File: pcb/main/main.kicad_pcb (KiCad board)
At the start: 2 copper layers, 172.1 x 109.2 mm, 74 parts, among them J1 Conn_01x04, J10 JTAG, J2 USB_B, J3 Trackball_conn, J4 ROW0, J5 RJ45, J6 ROW1, J7 ROW2, J8 ROW3, J9 STLink, SW1 SW40, SW2 SW41, SW3 SW42, SW4 SW43, SW5 RST_SW, SW6 BOOT0, SW7 BOOT1, U1 3.3v regul, U2 STM32F103C8Tx, Y1 32.768kHz, Y2 8MHz

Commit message: keyboard pcb
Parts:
- added G***: LOGO, folivora:logo, B.Cu at (189.2, 124.5)
- added G***: LOGO, folivora:logo, F.Cu at (172.7, 78.7)
- added G***: LOGO, folivora:logo, F.Cu at (189.2, 61.0)
- added G***: LOGO, folivora:logo, F.Cu at (189.2, 124.5)
- D5, D6, D7: footprint LED_THT:LED_D3.0mm -> LED_SMD:LED_1206_3216Metric
- moved D5 17.1 mm to (104.8, 105.4), turned to 180 degrees
- moved REF** 12.4 mm to (105.4, 90.2)
- moved D6 10.0 mm to (104.8, 102.9), turned to 180 degrees
- moved J10 5.59 mm to (216.4, 161.0)
- moved D7 3.25 mm to (104.8, 100.3), turned to 180 degrees
- moved R2 2.29 mm to (106.7, 109.2)
- moved J3 1.85 mm to (154.9, 153.0)
- moved R1 1.52 mm to (104.8, 109.2)
- moved C10 0.28 mm to (112.3, 123.4), turned to 90 degrees
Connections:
- J3 pad 1: +3V3 -> GND
- J3 pad 2: /SS_T -> /MOSI
- J3 pad 3: /SCK -> /MISO
- J3 pad 4: /MISO -> /SCK
- J3 pad 5: /MOSI -> /SS_T
- J3 pad 6: GND -> +3V3
- JP12 pad 1: +5V -> +3V3
- JP15 pad 1: +5V -> +3V3
- U2 pad 21: /LED3 -> Net-(U2-Pad21)
- U2 pad 22: /D- -> /READ5
- U2 pad 25: /D+ -> /READ4
- U2 pad 32: /READ5 -> /D-
- U2 pad 33: /READ4 -> /D+
- U2 pad 41: Net-(U2-Pad41) -> /LED3
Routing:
- net GND: track 0.00 -> 364.3 mm, vias 0 -> 11
- net +3V3: track 0.00 -> 345.9 mm, vias 0 -> 12
- net /READ0: track 80.8 -> 272.5 mm, vias 1 -> 7
- net /READ1: track 79.4 -> 269.4 mm, vias 2 -> 16
- net /RST: track 0.00 -> 184.1 mm, vias 0 -> 10
- net /SELECT1: track 0.00 -> 172.8 mm, vias 0 -> 2
- net /READ2: track 83.4 -> 254.0 mm, vias 0 -> 12
- net /READ3: track 86.7 -> 250.9 mm, vias 0 -> 5
- net /SELECT2: track 0.00 -> 161.7 mm, vias 0 -> 9
- net /SELECT4: track 0.00 -> 159.2 mm, vias 0 -> 4
- net /SELECT3: track 0.00 -> 156.6 mm, vias 0 -> 5
- net +5V: track 0.00 -> 154.1 mm, vias 0 -> 8
- net /JTDO: track 0.00 -> 148.1 mm, vias 0 -> 6
- net /BOOT1: track 0.00 -> 146.2 mm, vias 0 -> 2
- net /BOOT0: track 0.00 -> 146.0 mm, vias 0 -> 8
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- added copper zone on B.Cu, net GND
- added copper zone on F.Cu, net GND
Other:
- outline, holes or cut-outs redrawn
- rule trace_min: 0.2 -> 0
- board text added: "0.1uF"
- board text added: "10Mohm"
- board text added: "10kohm"
- board text added: "10uF"
- board text added: "220ohm"
- board text added: "32.768kHz"
- board text added: "8MHz"
- board text added: "<-D"
- board text added: "BOOT0"
- board text added: "BOOT1"
- board text added: "D->"
- board text added: "Fill all if this is ride side"
- board text added: "JTAG 10pin"
- board text added: "RJ45"
- board text added: "RST"
- board text added: "STLink"
- board text added: "STM32F103C8Tx"
- board text added: "Trackball"
- board text added: "USB B"
- board text added: "to 3.3v"

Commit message: fix design
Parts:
- removed the REF** at (263.5, 147.3)
- removed the REF** at (263.5, 128.3)
- removed the REF** at (125.7, 90.2)
- added REF**: MountingHole_2.2mm_M2, MountingHole:MountingHole_2.2mm_M2, F.Cu at (55.9, 72.4)
- added REF**: MountingHole_2.2mm_M2, MountingHole:MountingHole_2.2mm_M2, F.Cu at (74.9, 59.7)
- added REF**: MountingHole_2.2mm_M2, MountingHole:MountingHole_2.2mm_M2, F.Cu at (113.0, 59.7)
- added REF**: MountingHole_2.2mm_M2, MountingHole:MountingHole_2.2mm_M2, F.Cu at (113.0, 72.4)
- added REF**: MountingHole_2.2mm_M2, MountingHole:MountingHole_2.2mm_M2, F.Cu at (55.9, 53.3)
- added REF**: MountingHole_2.2mm_M2, MountingHole:MountingHole_2.2mm_M2, F.Cu at (132.1, 40.6)
- added REF**: MountingHole_2.2mm_M2, MountingHole:MountingHole_2.2mm_M2, F.Cu at (94.0, 53.3)
- added REF**: MountingHole_2.2mm_M2, MountingHole:MountingHole_2.2mm_M2, F.Cu at (94.0, 40.6)
- added REF**: MountingHole_2.2mm_M2, MountingHole:MountingHole_2.2mm_M2, F.Cu at (151.1, 53.3)
- added REF**: MountingHole_2.2mm_M2, MountingHole:MountingHole_2.2mm_M2, F.Cu at (55.9, 40.6)
- added REF**: MountingHole_2.2mm_M2, MountingHole:MountingHole_2.2mm_M2, F.Cu at (151.1, 40.6)
- added REF**: MountingHole_2.2mm_M2, MountingHole:MountingHole_2.2mm_M2, F.Cu at (132.1, 59.7)
- added REF**: MountingHole_2.2mm_M2, MountingHole:MountingHole_2.2mm_M2, F.Cu at (132.1, 53.3)
- added REF**: MountingHole_2.2mm_M2, MountingHole:MountingHole_2.2mm_M2, F.Cu at (74.9, 53.3)
- added REF**: MountingHole_2.2mm_M2, MountingHole:MountingHole_2.2mm_M2, F.Cu at (74.9, 40.6)
- added REF**: MountingHole_2.2mm_M2, MountingHole:MountingHole_2.2mm_M2, F.Cu at (113.0, 40.6)
- added REF**: MountingHole_2.2mm_M2, MountingHole:MountingHole_2.2mm_M2, F.Cu at (113.0, 53.3)
- added REF**: MountingHole_2.2mm_M2, MountingHole:MountingHole_2.2mm_M2, F.Cu at (55.9, 34.3)
- added REF**: MountingHole_2.2mm_M2, MountingHole:MountingHole_2.2mm_M2, F.Cu at (132.1, 21.6)
- added REF**: MountingHole_2.2mm_M2, MountingHole:MountingHole_2.2mm_M2, F.Cu at (94.0, 34.3)
- added REF**: MountingHole_2.2mm_M2, MountingHole:MountingHole_2.2mm_M2, F.Cu at (94.0, 21.6)
- added REF**: MountingHole_2.2mm_M2, MountingHole:MountingHole_2.2mm_M2, F.Cu at (151.1, 34.3)
- added REF**: MountingHole_2.2mm_M2, MountingHole:MountingHole_2.2mm_M2, F.Cu at (94.0, 72.4)
- added REF**: MountingHole_2.2mm_M2, MountingHole:MountingHole_2.2mm_M2, F.Cu at (55.9, 21.6)
- added REF**: MountingHole_2.2mm_M2, MountingHole:MountingHole_2.2mm_M2, F.Cu at (151.1, 21.6)
- added REF**: MountingHole_2.2mm_M2, MountingHole:MountingHole_2.2mm_M2, F.Cu at (132.1, 34.3)
- added REF**: MountingHole_2.2mm_M2, MountingHole:MountingHole_2.2mm_M2, F.Cu at (74.9, 34.3)
- added REF**: MountingHole_2.2mm_M2, MountingHole:MountingHole_2.2mm_M2, F.Cu at (74.9, 21.6)
- added REF**: MountingHole_2.2mm_M2, MountingHole:MountingHole_2.2mm_M2, F.Cu at (113.0, 21.6)
- added REF**: MountingHole_2.2mm_M2, MountingHole:MountingHole_2.2mm_M2, F.Cu at (113.0, 34.3)
- added REF**: MountingHole_2.2mm_M2, MountingHole:MountingHole_2.2mm_M2, F.Cu at (94.0, 59.7)
- added REF**: MountingHole_3.2mm_M3, MountingHole:MountingHole_3.2mm_M3, F.Cu at (161.9, 66.0)
- added REF**: MountingHole_3.2mm_M3, MountingHole:MountingHole_3.2mm_M3, F.Cu at (161.9, 47.0)
- added REF**: MountingHole_3.2mm_M3, MountingHole:MountingHole_3.2mm_M3, F.Cu at (24.1, 5.08)
- added REF**: MountingHole_2.2mm_M2, MountingHole:MountingHole_2.2mm_M2, F.Cu at (55.9, 15.2)
- added REF**: MountingHole_2.2mm_M2, MountingHole:MountingHole_2.2mm_M2, F.Cu at (151.1, 72.4)
- added REF**: MountingHole_2.2mm_M2, MountingHole:MountingHole_2.2mm_M2, F.Cu at (55.9, 2.54)
- added REF**: MountingHole_2.2mm_M2, MountingHole:MountingHole_2.2mm_M2, F.Cu at (74.9, 2.54)
- added REF**: MountingHole_2.2mm_M2, MountingHole:MountingHole_2.2mm_M2, F.Cu at (74.9, 15.2)
- added REF**: MountingHole_2.2mm_M2, MountingHole:MountingHole_2.2mm_M2, F.Cu at (94.0, 2.54)
- added REF**: MountingHole_2.2mm_M2, MountingHole:MountingHole_2.2mm_M2, F.Cu at (94.0, 15.2)
- added REF**: MountingHole_2.2mm_M2, MountingHole:MountingHole_2.2mm_M2, F.Cu at (113.0, 2.54)
- added REF**: MountingHole_2.2mm_M2, MountingHole:MountingHole_2.2mm_M2, F.Cu at (113.0, 15.2)
- added REF**: MountingHole_2.2mm_M2, MountingHole:MountingHole_2.2mm_M2, F.Cu at (55.9, 59.7)
- added REF**: MountingHole_2.2mm_M2, MountingHole:MountingHole_2.2mm_M2, F.Cu at (151.1, 59.7)
- added REF**: MountingHole_2.2mm_M2, MountingHole:MountingHole_2.2mm_M2, F.Cu at (132.1, 72.4)
- added REF**: MountingHole_2.2mm_M2, MountingHole:MountingHole_2.2mm_M2, F.Cu at (74.9, 72.4)
- J4, J6, J7, J8: footprint Connector_JST:JST_XH_S07B-XH-A_1x07_P2.50mm_Horizontal -> Connector_PinSocket_2.00mm:PinSocket_1x07_P2.00mm_Vertical; moved to F.Cu
- SW6, SW7: footprint Button_Switch_THT:SW_E-Switch_EG1224_SPDT_Angled -> Button_Switch_THT:SW_CuK_OS102011MA1QN1_SPDT_Angled
- moved J3 155.8 mm to (21.6, 72.4), turned to 270 degrees
- moved U1 150.0 mm to (19.7, 59.1), turned to 45 degrees
- moved C2 145.1 mm to (15.2, 64.8), turned to 135 degrees
- moved C1 144.7 mm to (10.8, 64.8), turned to 315 degrees
- moved J4 134.3 mm to (132.1, 3.17), turned to 0 degrees
- moved REF** 132.5 mm to (3.81, 5.08)
- moved J2 131.0 mm to (12.7, 16.0)
- moved J6 130.6 mm to (168.3, 21.6), turned to 0 degrees
- moved C5 130.1 mm to (6.35, 47.4)
- moved D5 130.1 mm to (3.17, 24.1)
- moved D6 130.1 mm to (3.17, 21.6)
- moved D7 130.1 mm to (3.17, 19.1)
- moved J1 130.1 mm to (10.2, 21.8)
- moved J9 130.1 mm to (95.5, 79.8)
- moved JP10 130.1 mm to (10.2, 25.7)
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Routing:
- net +3V3: track 345.9 -> 289.7 mm, vias 12 -> 16
- net /MOSI: track 81.3 -> 42.6 mm, vias 2 -> 0
- net /READ5: track 205.5 -> 243.8 mm, vias 2 -> 1
- net /MISO: track 90.1 -> 55.2 mm
- net /READ1: track 269.4 -> 299.2 mm, vias 16 -> 5
- net /READ4: track 208.3 -> 232.3 mm, vias 2 -> 4
- net /READ2: track 254.0 -> 276.7 mm, vias 12 -> 6
- net /SCK: track 86.1 -> 63.6 mm, vias 1 -> 2
- net /SWCLK: track 135.4 -> 155.7 mm, vias 4 -> 1
- net /SS_T: track 81.1 -> 64.3 mm, vias 3 -> 2
- net /JNTRST: track 142.2 -> 126.0 mm, vias 6 -> 1
- net /JTDO: track 148.1 -> 132.9 mm, vias 6 -> 1
- net GND: track 364.3 -> 350.5 mm, vias 11 -> 13
- net /READ3: track 250.9 -> 262.7 mm, vias 5 -> 8
- net /SELECT1: track 172.8 -> 163.0 mm, vias 2 -> 1
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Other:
- board size 172.1 x 109.2 mm -> 172.1 x 113 mm
- net class Default: clearance 0.2 -> 0.16; trace_width 0.25 -> 0.2; via_dia 0.8 -> 0.5; via_drill 0.4 -> 0.3
- rule trace_clearance: 0.2 -> 0.16

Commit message: complete pcb design
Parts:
- removed D1, D2, D3, D4: D, Diode_SMD:D_SOD-123
- removed the G*** at (94.0, 44.5) (x2)
- removed J10: JTAG, Connector_PinSocket_2.54mm:PinSocket_2x05_P2.54mm_Horizontal
- removed J9: STLink, Connector_PinSocket_2.54mm:PinSocket_2x05_P2.54mm_Horizontal
- removed REF** (x44): MountingHole_2.2mm_M2, MountingHole:MountingHole_2.2mm_M2
- removed REF** (x12): MountingHole_3.2mm_M3, MountingHole:MountingHole_3.2mm_M3
- removed SW1: SW40, folivora:SW_Cherry_MX1A_1.00u_PCB
- removed SW2: SW41, folivora:SW_Cherry_MX1A_1.00u_PCB
- removed SW3: SW42, folivora:SW_Cherry_MX1A_1.00u_PCB
- removed SW4: SW43, folivora:SW_Cherry_MX1A_1.00u_PCB
- J3: value Trackball_conn -> Serial; footprint Connector_JST:JST_XH_S06B-XH-A_1x06_P2.50mm_Horizontal -> Connector_PinHeader_2.54mm:PinHeader_1x04_P2.54mm_Vertical; moved to F.Cu
- J4: value ROW0 -> STLink; footprint Connector_PinSocket_2.00mm:PinSocket_1x07_P2.00mm_Vertical -> Connector_PinHeader_2.54mm:PinHeader_1x04_P2.54mm_Vertical
- J6: value ROW1 -> SELECT; footprint Connector_PinSocket_2.00mm:PinSocket_1x07_P2.00mm_Vertical -> Connector_PinSocket_2.54mm:PinSocket_1x05_P2.54mm_Vertical
- J7: value ROW2 -> READ; footprint Connector_PinSocket_2.00mm:PinSocket_1x07_P2.00mm_Vertical -> Connector_PinSocket_2.54mm:PinSocket_1x06_P2.54mm_Vertical
- J8: value ROW3 -> TRACKBALL; footprint Connector_PinSocket_2.00mm:PinSocket_1x07_P2.00mm_Vertical -> Connector_PinSocket_2.54mm:PinSocket_1x06_P2.54mm_Vertical
- JP10, JP12, JP14, JP16: moved to F.Cu
- JP11, JP13, JP15, JP17: moved to B.Cu
- Y1: footprint Crystal:Crystal_DS15_D1.5mm_L5.0mm_Vertical -> Crystal:Crystal_SMD_3215-2Pin_3.2x1.5mm
- Y2: footprint Crystal:Crystal_HC49-U_Vertical -> Crystal:Crystal_SMD_Abracon_ABM3-2Pin_5.0x3.2mm
- moved D5 135.0 mm to (88.3, 128.9), turned to 0 degrees
- moved D6 135.0 mm to (88.3, 126.4), turned to 0 degrees
- moved D7 135.0 mm to (88.3, 123.8), turned to 0 degrees
- moved R1 134.8 mm to (89.5, 131.4), turned to 180 degrees
- moved R3 132.4 mm to (92.6, 123.8), turned to 180 degrees
- moved R2 131.4 mm to (92.1, 126.4), turned to 180 degrees
- moved J1 120.9 mm to (80.6, 120.0)
- moved SW5 116.6 mm to (70.5, 146.1), turned to 90 degrees
- moved JP10 115.3 mm to (80.6, 116.8), turned to 270 degrees
- moved JP11 115.3 mm to (80.6, 116.8), turned to 270 degrees
- moved JP12 115.3 mm to (83.2, 116.8), turned to 270 degrees
- moved JP13 115.3 mm to (83.2, 116.8), turned to 270 degrees
- moved JP14 115.3 mm to (85.7, 116.8), turned to 270 degrees
- moved JP15 115.3 mm to (85.7, 116.8), turned to 270 degrees
- moved JP16 115.3 mm to (88.3, 116.8), turned to 270 degrees
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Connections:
- net /SS_K renamed /SS
- J3 pad 2: /MOSI -> /RX
- J3 pad 3: /MISO -> /TX
- J3 pad 4: /SCK -> +3V3
- J4 pad 1: /SELECT0 -> GND
- J4 pad 2: /READ0 -> /SWCLK
- J4 pad 3: /READ1 -> /SWDIO
- J4 pad 4: /READ2 -> +3V3
- J5 pad 2: Net-(J5-Pad2) -> GND
- J5 pad 7: /SS_T -> +3V3
- J6 pad 1: /SELECT1 -> /SELECT0
- J6 pad 2: /READ0 -> /SELECT1
- J6 pad 3: /READ1 -> /SELECT2
- J6 pad 4: /READ2 -> /SELECT3
- J6 pad 5: /READ3 -> /SELECT4
- J7 pad 1: /SELECT2 -> /READ0
- J7 pad 2: /READ0 -> /READ1
- J7 pad 3: /READ1 -> /READ2
- J7 pad 4: /READ2 -> /READ3
- J7 pad 5: /READ3 -> /READ4
- J7 pad 6: /READ4 -> /READ5
- J8 pad 1: /SELECT3 -> +3V3
- J8 pad 2: /READ0 -> /UP
- J8 pad 3: /READ1 -> /DOWN
- J8 pad 4: /READ2 -> /RIGHT
- J8 pad 5: /READ3 -> /LEFT
- J8 pad 6: /READ4 -> GND
- U2 pad 10: /SELECT0 -> /LED1
- U2 pad 11: /SELECT1 -> /LED2
- U2 pad 12: /SELECT2 -> /LED3
- U2 pad 13: /SS_T -> Net-(U2-Pad13)
- U2 pad 18: Net-(U2-Pad18) -> /SELECT4
- U2 pad 19: Net-(U2-Pad19) -> /SELECT3
- U2 pad 21: Net-(U2-Pad21) -> /SELECT1
- U2 pad 22: /READ5 -> /SELECT0
- U2 pad 25: /READ4 -> /LEFT
- U2 pad 26: /READ3 -> /RIGHT
- U2 pad 27: /READ2 -> /DOWN
- U2 pad 28: /READ1 -> /UP
- U2 pad 29: /JTDI -> /SELECT2
- U2 pad 30: /SELECT3 -> /TX
- U2 pad 31: /SELECT4 -> /RX
- U2 pad 38: /READ0 -> /READ5
- U2 pad 39: /JTDO -> /READ4
- U2 pad 40: /JNTRST -> /READ3
- U2 pad 41: /LED3 -> /READ2
- U2 pad 45: /LED1 -> /READ1
- U2 pad 46: /LED2 -> /READ0
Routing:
- net /READ1: track 299.2 -> 33.4 mm, vias 5 -> 1
- net /READ2: track 276.7 -> 29.9 mm, vias 6 -> 1
- net /READ0: track 277.8 -> 36.5 mm, vias 7 -> 1
- net /READ3: track 262.7 -> 27.0 mm, vias 8 -> 1
- net /READ5: track 243.8 -> 21.4 mm
- net /READ4: track 232.3 -> 24.2 mm, vias 4 -> 1
- net /SELECT1: track 163.0 -> 19.2 mm
- net /BOOT0: track 152.9 -> 14.2 mm, vias 6 -> 2
- net /SELECT2: track 155.7 -> 17.2 mm
- net /SELECT4: track 161.4 -> 27.3 mm, vias 2 -> 1
- net /SELECT3: track 158.4 -> 24.5 mm, vias 5 -> 1
- net /JTDO: track 132.9 -> 0.00 mm, vias 1 -> 0
- net /RST: track 178.5 -> 46.4 mm, vias 5 -> 2
- net +5V: track 151.3 -> 21.9 mm, vias 6 -> 3
- net /JNTRST: track 126.0 -> 0.00 mm, vias 1 -> 0
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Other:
- board size 172.1 x 113 mm -> 29.4 x 103.3 mm
- board text removed: "0.1uF"
- board text removed: "10Mohm"
- board text removed: "10kohm"
- board text removed: "10uF"
- board text removed: "220ohm"
- board text removed: "32.768kHz"
- board text removed: "8MHz"
- board text removed: "<-D"
- board text removed: "BOOT0"
- board text removed: "BOOT1"
- board text removed: "D->"
- board text removed: "Fill all if this is ride side"
- board text removed: "JTAG 10pin"
- board text removed: "RJ45"
- board text removed: "RST"
- board text removed: "STLink"
- board text removed: "STM32F103C8Tx"
- board text removed: "Trackball"
- board text removed: "USB B"
- board text removed: "to 3.3v"

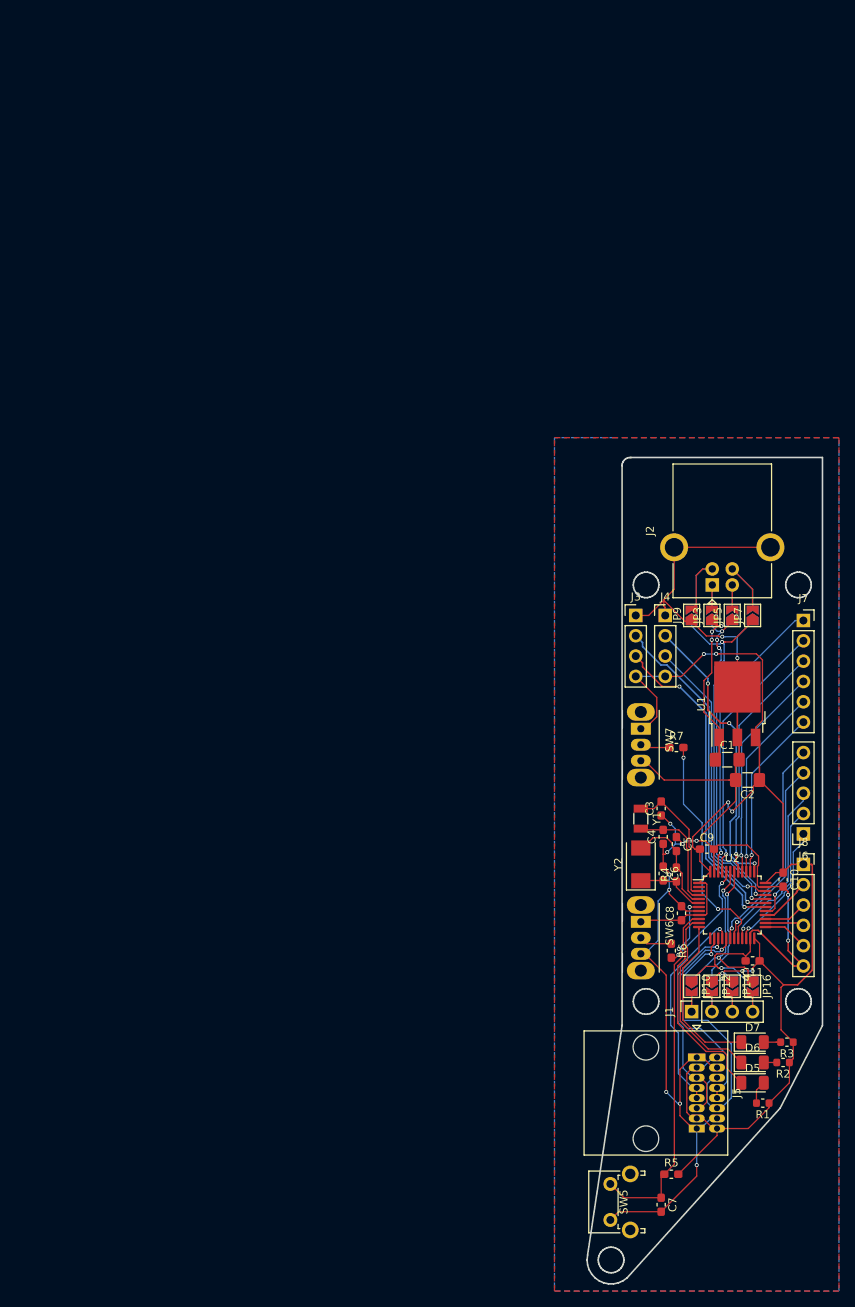
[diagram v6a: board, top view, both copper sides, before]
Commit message: resize main pcb
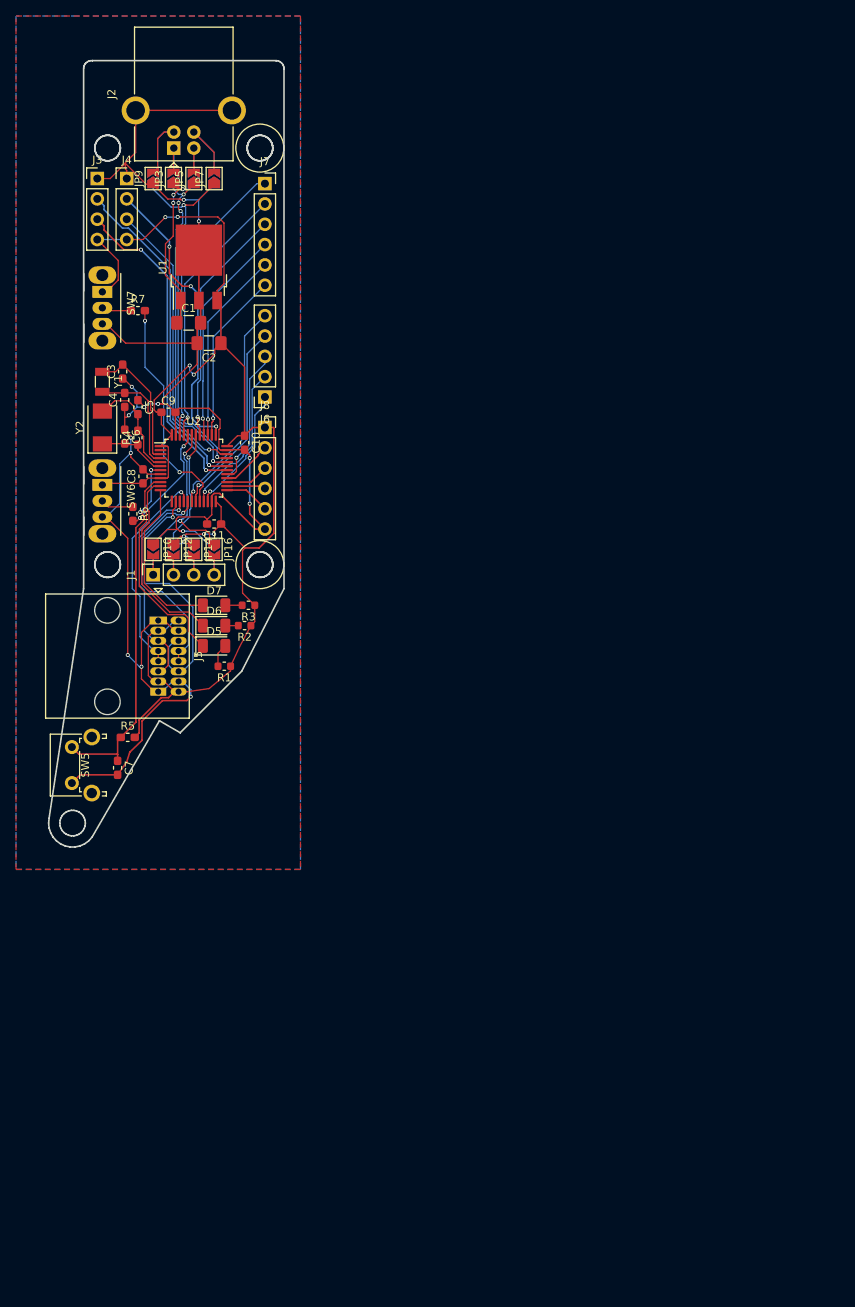
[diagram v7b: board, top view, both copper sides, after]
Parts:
- moved R5 87.2 mm to (10.2, 85.7)
- moved C7 87.2 mm to (8.89, 89.5)
- moved C1 86.7 mm to (17.8, 33.9)
- moved C11 86.7 mm to (21.0, 59.1)
- moved J6 86.7 mm to (27.3, 43.2)
- moved JP10 86.7 mm to (13.3, 62.2)
- moved JP11 86.7 mm to (13.3, 62.2)
- moved JP12 86.7 mm to (15.9, 62.2)
- moved JP13 86.7 mm to (15.9, 62.2)
- moved JP14 86.7 mm to (18.4, 62.2)
- moved JP15 86.7 mm to (18.4, 62.2)
- moved JP16 86.7 mm to (21.0, 62.2)
- moved JP17 86.7 mm to (21.0, 62.2)
- moved R4 86.7 mm to (11.4, 48.3)
- moved R7 86.7 mm to (11.4, 32.4)
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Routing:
- net GND: track 225.4 -> 230.5 mm
- net /RST: track 46.4 -> 45.7 mm
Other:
- board size 29.4 x 103.3 mm -> 29.4 x 98.3 mm
